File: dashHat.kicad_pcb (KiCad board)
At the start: 4 copper layers, 65 x 56 mm, 114 parts, among them J1 Input, J2 LCD, J3 GPIO, J4 LEDs, J5 SMA, J6 Ride Through, Q1 BSS138, Q2 BSS138, Q3 2N7002, Q4 BSS84, Q5 BSS84, Q6 BSS84, U1 CAT24C256, U2 MAX17614, U3 TVS3300DRV, U4 LM61480, U5 74LVC1G80, U6 ZOE-M8Q, U7 TCAN330, U8 MCP2515-xST, U9 MAX3227, Y1 32.768k, Y2 8MHz

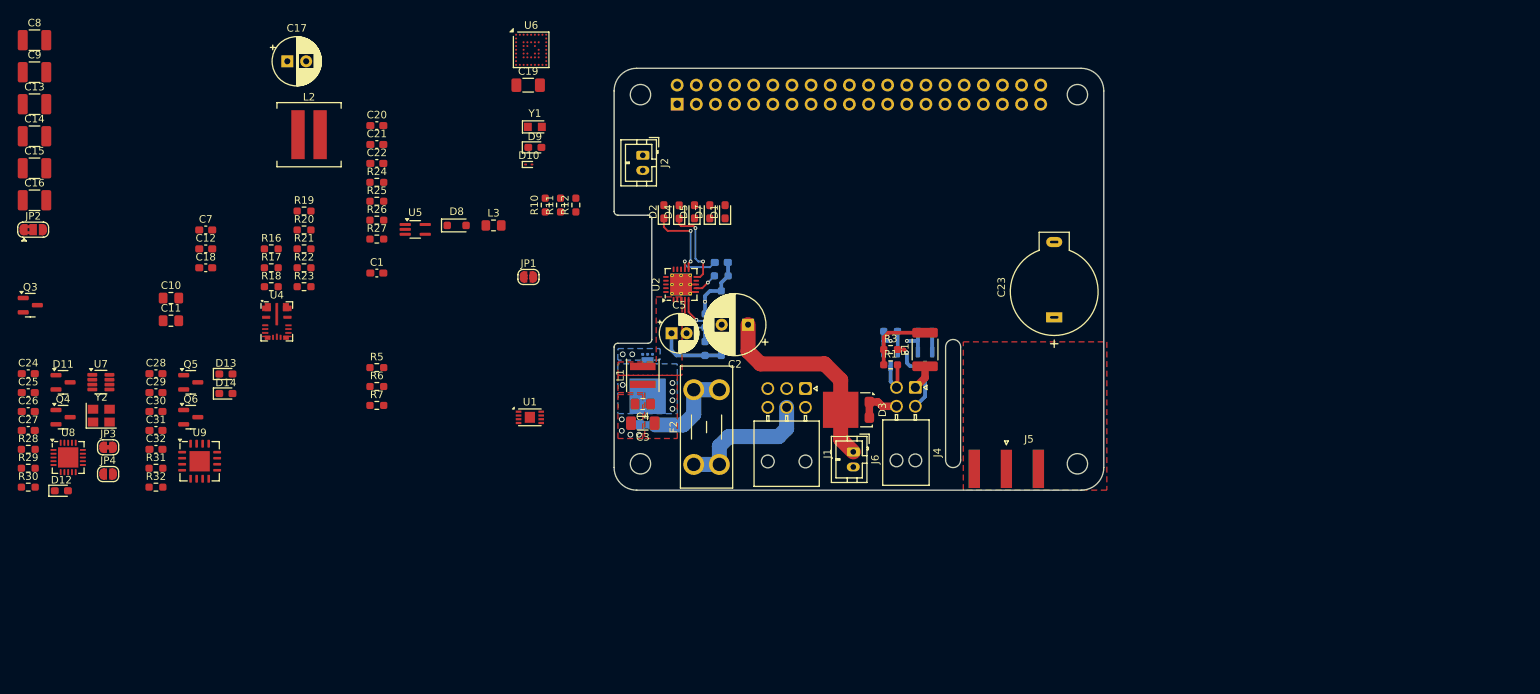
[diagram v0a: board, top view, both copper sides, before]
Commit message: added 4 inputs and 2 pwm outputs, completed routing
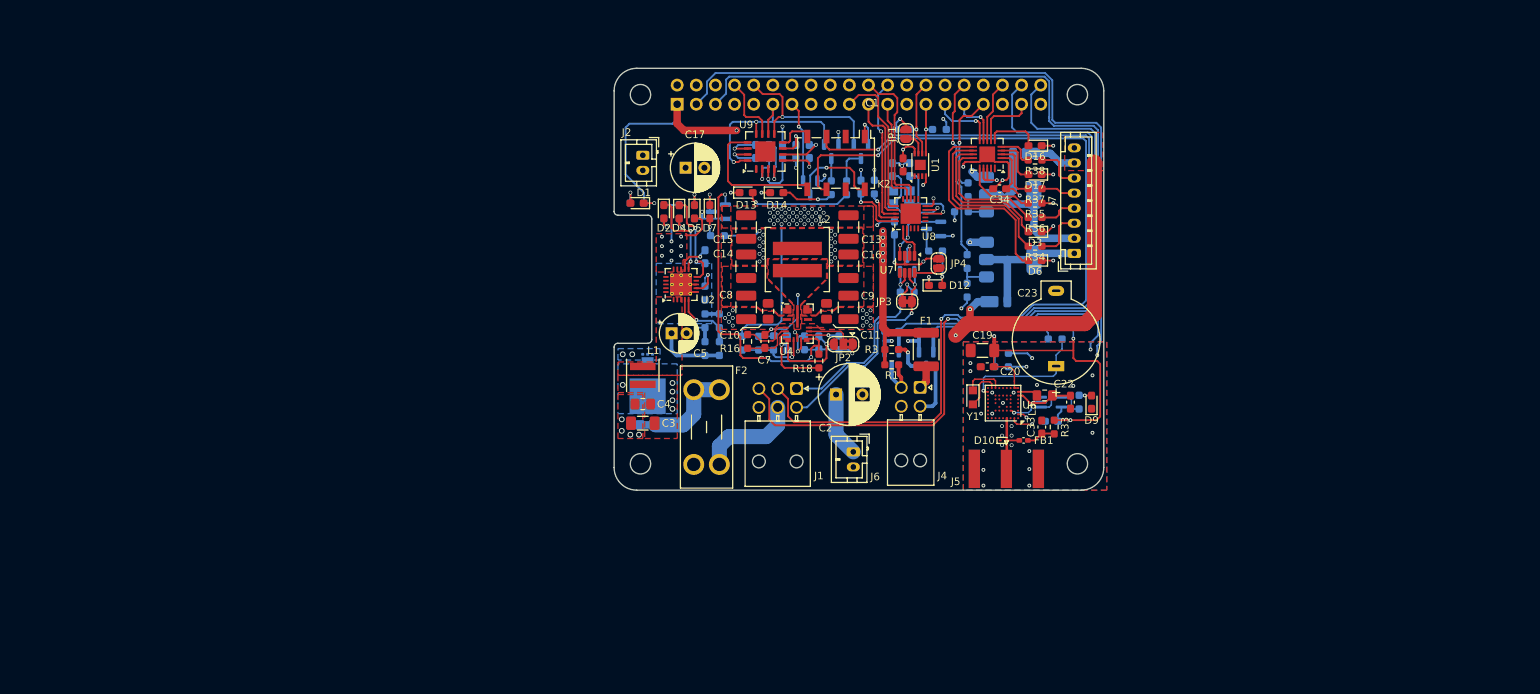
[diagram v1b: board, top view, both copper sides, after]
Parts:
- added C33: 47p, Capacitor_SMD:C_0603_1608Metric_Pad1.08x0.95mm_HandSolder, F.Cu at (156.8, 91.6)
- added C34: 0.1u, Capacitor_SMD:C_0603_1608Metric_Pad1.08x0.95mm_HandSolder, F.Cu at (151.2, 60.0)
- added D16: Green, LED_SMD:LED_0603_1608Metric_Pad1.05x0.95mm_HandSolder, F.Cu at (155.9, 54.3)
- added D17: Green, LED_SMD:LED_0603_1608Metric_Pad1.05x0.95mm_HandSolder, F.Cu at (155.9, 58.1)
- added D18: 60v, 3A, Diode_SMD:D_PowerDI-123, B.Cu at (154.5, 55.3)
- added D19: 60v, 3A, Diode_SMD:D_PowerDI-123, B.Cu at (150.7, 75.0)
- added D6: Green, LED_SMD:LED_0603_1608Metric_Pad1.05x0.95mm_HandSolder, F.Cu at (155.9, 69.5)
- added FB1: 1.8k @ 100MHz, Inductor_SMD:L_0402_1005Metric_Pad0.77x0.64mm_HandSolder, F.Cu at (154.4, 93.4)
- added J7: Conn_01x08, Connector_JST:JST_PH_B8B-PH-K_1x08_P2.00mm_Vertical, F.Cu at (161.1, 68.6)
- added K2: G6K-2, Relay_SMD:Relay_DPDT_Omron_G6K-2F, F.Cu at (129.5, 56.6)
- added Q7: 2N7002, Package_TO_SOT_SMD:SOT-23, B.Cu at (126.0, 59.9)
- added Q8: , Package_TO_SOT_SMD:SOT-223, B.Cu at (152.6, 60.8)
- added Q9: , Package_TO_SOT_SMD:SOT-223, B.Cu at (152.6, 69.4)
- added R33: 10, Resistor_SMD:R_0603_1608Metric_Pad0.98x0.95mm_HandSolder, F.Cu at (158.4, 91.6)
- added R34: 1.5k, Resistor_SMD:R_0603_1608Metric_Pad0.98x0.95mm_HandSolder, F.Cu at (155.9, 67.6)
- added R35: 18k, Resistor_SMD:R_0603_1608Metric_Pad0.98x0.95mm_HandSolder, F.Cu at (155.9, 61.9)
- added R36: 1.5k, Resistor_SMD:R_0603_1608Metric_Pad0.98x0.95mm_HandSolder, F.Cu at (155.9, 63.8)
- added R37: 1.5k, Resistor_SMD:R_0603_1608Metric_Pad0.98x0.95mm_HandSolder, F.Cu at (155.9, 60.0)
- added R38: 1.5k, Resistor_SMD:R_0603_1608Metric_Pad0.98x0.95mm_HandSolder, F.Cu at (155.9, 56.2)
- added R39: 50, Resistor_SMD:R_0603_1608Metric_Pad0.98x0.95mm_HandSolder, B.Cu at (147.0, 60.1)
- added R40: 10k, Resistor_SMD:R_0603_1608Metric_Pad0.98x0.95mm_HandSolder, B.Cu at (146.1, 63.0)
- added R41: 50, Resistor_SMD:R_0603_1608Metric_Pad0.98x0.95mm_HandSolder, B.Cu at (146.9, 69.6)
- added R42: 10k, Resistor_SMD:R_0603_1608Metric_Pad0.98x0.95mm_HandSolder, B.Cu at (146.9, 73.5)
- added U10: MAX22193, Package_DFN_QFN:TQFN-20-1EP_4x4mm_P0.5mm_EP2.1x2.1mm, F.Cu at (149.5, 55.4)
- C12, C18, C21, C24, C25, C26, C27, C28, C29, C30, C31, C32, D11, D8, Q3, Q4, Q5, Q6, R10, R11, R12, R17, R19, R20, R21, R22, R23, R24, R25, R26, R27, R28, R29, R30, R31, R32, R5, R6, R7, U5, Y2: moved to B.Cu
- C6: value 220n -> 1u
- D3: value 100v, 15A -> Green; footprint Package_TO_SOT_SMD:TO-277A -> LED_SMD:LED_0603_1608Metric_Pad1.05x0.95mm_HandSolder
- moved R30 124.5 mm to (142.7, 68.2)
- moved C25 120.7 mm to (139.2, 57.5), turned to 90 degrees
- moved D12 119.2 mm to (142.7, 72.8)
- moved C26 119.1 mm to (137.0, 57.5), turned to 90 degrees
- moved R28 118.5 mm to (138.9, 73.7), turned to 180 degrees
- moved R29 118.4 mm to (134.5, 59.8), turned to 90 degrees
- moved Q4 118.2 mm to (142.4, 65.3), turned to 180 degrees
- moved C24 116.6 mm to (137.2, 65.2), turned to 90 degrees
- moved U8 116.4 mm to (139.4, 63.3), turned to 90 degrees
- moved C27 115.2 mm to (132.8, 59.8), turned to 90 degrees
- moved JP4 113.7 mm to (143.1, 69.9), turned to 90 degrees
- moved D11 113.1 mm to (138.9, 70.0), turned to 90 degrees
- moved C9 112.5 mm to (131.1, 75.7), turned to 90 degrees
- moved Y2 110.1 mm to (138.1, 61.1), turned to 180 degrees
- moved C13 109.3 mm to (131.1, 65.1), turned to 90 degrees
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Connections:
- C10 pad 1: +12V -> VIN
- C11 pad 1: +12V -> VIN
- C2 pad 1: +12V -> VIN
- C8 pad 1: +12V -> VIN
- C9 pad 1: +12V -> VIN
- D3 pad 1: +12V -> GND
- D3 pad 2: GND -> Net-(D3-A)
- D5 pad 1: GND -> Net-(D5-K)
- D5 pad 2: Net-(D5-A) -> VIN
- F2 pad 1: /Power/+12Vraw -> /Power/+12V_{raw}
- J1 pad 1: /RS232/232TX -> /CAN/CANL
- J1 pad 2: /RS232/232RX -> /RS232/232TX
- J1 pad 3: /CAN/CANH -> /RS232/232RX
- J1 pad 4: /CAN/CANL -> /CAN/CANH
- J1 pad 5: /Power/+12Vraw -> /GPIO/+12V_{raw}
- J6 pad 1: +12V -> VIN
- R10 pad 1: +12V -> VIN
- R11 pad 1: +12V -> VIN
- R12 pad 1: +12V -> Net-(D5-K)
- R12 pad 2: Net-(D5-A) -> GND
- U2 pad 13: +12V -> VIN
- U2 pad 14: +12V -> VIN
- U2 pad 15: +12V -> VIN
- U4 pad 13: +12V -> VIN
- U4 pad 14: +12V -> VIN
- U4 pad 2: +12V -> VIN
- U9 pad 13: /RS232/232TX -> Net-(U9-T1OUT)
- U9 pad 8: /RS232/232RX -> Net-(U9-R1IN)
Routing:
- net +3V3: track 7.94 -> 147.6 mm, vias 2 -> 19
- net /RS232/232TX: track 0.00 -> 121.4 mm, vias 0 -> 2
- net /RS232/232RX: track 0.00 -> 120.6 mm, vias 0 -> 2
- net /GPIO2/SDA1: track 0.00 -> 116.8 mm, vias 0 -> 3
- net /GPIO3/SCL1: track 0.00 -> 110.0 mm, vias 0 -> 3
- net /GPIO/+12V_{raw}: track 0.00 -> 102.4 mm, vias 0 -> 2
- net +5V: track 9.39 -> 106.3 mm, vias 0 -> 24
- net GND: track 19.4 -> 95.3 mm, vias 7 -> 94
- net VIN: track 0.00 -> 70.8 mm, vias 0 -> 23
- net /GPIO20/PCM.DIN: track 2.76 -> 69.5 mm
- net /GPIO21/PCM.DOUT: track 2.76 -> 63.3 mm
- net Net-(Q3-G): track 0.00 -> 41.4 mm, vias 0 -> 3
- net /GPIO17: track 0.00 -> 30.7 mm, vias 0 -> 2
- net /CAN/CANH: track 0.00 -> 30.4 mm, vias 0 -> 2
- net +12V: track 27.7 -> 0.00 mm
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- added copper zone on In2.Cu, net +3V3
- added copper zone on F.Cu, net +5V
- added copper zone on In2.Cu, net +5V
- added copper zone on F.Cu, net /GPIO/+12V_{raw}
- added copper zone on F.Cu, net Net-(U4-SW)
- added copper zone on F.Cu, net VIN
- added copper zone on In2.Cu, net VIN
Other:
- outline, holes or cut-outs redrawn
- board text removed: "CAMERA (OPTIONAL)"

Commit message: revised schematic after initial layout  - all connectors are vertical  - increased current handling of outputs  - replaced mechanical relay with ssr  - jumper to disable gps antenna power
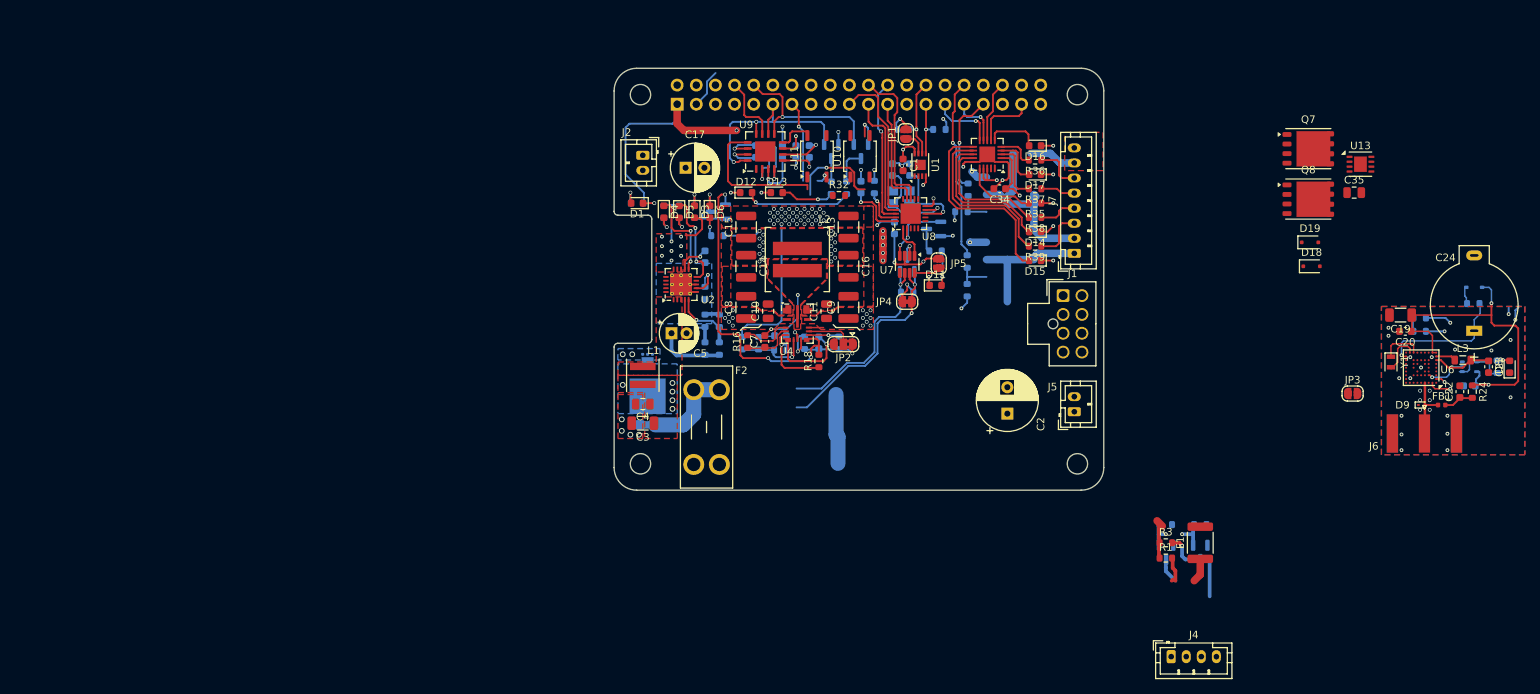
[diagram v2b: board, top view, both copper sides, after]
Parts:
- removed K2: G6K-2, Relay_SMD:Relay_DPDT_Omron_G6K-2F
- removed Q9: , Package_TO_SOT_SMD:SOT-223
- added C35: .47u, Capacitor_SMD:C_0805_2012Metric, F.Cu at (198.2, 60.5)
- added JP3: PA EN, Jumper:SolderJumper-2_P1.3mm_Open_RoundedPad1.0x1.5mm, F.Cu at (198.0, 87.2)
- added R32: 1k, Resistor_SMD:R_0603_1608Metric, F.Cu at (129.8, 60.9)
- added U10: CPC1017N, Package_SO:SOP-4_3.8x4.1mm_P2.54mm, F.Cu at (132.6, 55.7)
- added U11: CPC1017N, Package_SO:SOP-4_3.8x4.1mm_P2.54mm, F.Cu at (126.9, 55.7)
- added U13: IX4427, Package_DFN_QFN:DFN-8-1EP_3x3mm_P0.65mm_EP1.7x2.05mm, F.Cu at (199.1, 56.7)
- C1, C12, C18, C20, C21, C34, C6, C7: footprint Capacitor_SMD:C_0603_1608Metric_Pad1.08x0.95mm_HandSolder -> Capacitor_SMD:C_0603_1608Metric
- C10, C11, C4: footprint Capacitor_SMD:C_0805_2012Metric_Pad1.18x1.45mm_HandSolder -> Capacitor_SMD:C_0805_2012Metric
- C13, C14, C15, C16, C8, C9: footprint Capacitor_SMD:C_1210_3225Metric_Pad1.33x2.70mm_HandSolder -> Capacitor_SMD:C_1210_3225Metric
- C19, C3: footprint Capacitor_SMD:C_1206_3216Metric_Pad1.33x1.80mm_HandSolder -> Capacitor_SMD:C_1206_3216Metric
- C22: renamed from C33; footprint Capacitor_SMD:C_0603_1608Metric_Pad1.08x0.95mm_HandSolder -> Capacitor_SMD:C_0603_1608Metric
- C23: renamed from C22; footprint Capacitor_SMD:C_0603_1608Metric_Pad1.08x0.95mm_HandSolder -> Capacitor_SMD:C_0603_1608Metric
- C25: renamed from C24; footprint Capacitor_SMD:C_0603_1608Metric_Pad1.08x0.95mm_HandSolder -> Capacitor_SMD:C_0603_1608Metric
- C26: renamed from C25; footprint Capacitor_SMD:C_0603_1608Metric_Pad1.08x0.95mm_HandSolder -> Capacitor_SMD:C_0603_1608Metric
- C27: renamed from C26; footprint Capacitor_SMD:C_0603_1608Metric_Pad1.08x0.95mm_HandSolder -> Capacitor_SMD:C_0603_1608Metric
- C28: renamed from C27; footprint Capacitor_SMD:C_0603_1608Metric_Pad1.08x0.95mm_HandSolder -> Capacitor_SMD:C_0603_1608Metric
- C29: renamed from C28; footprint Capacitor_SMD:C_0603_1608Metric_Pad1.08x0.95mm_HandSolder -> Capacitor_SMD:C_0603_1608Metric
- C30: renamed from C29; footprint Capacitor_SMD:C_0603_1608Metric_Pad1.08x0.95mm_HandSolder -> Capacitor_SMD:C_0603_1608Metric
- C31: renamed from C30; footprint Capacitor_SMD:C_0603_1608Metric_Pad1.08x0.95mm_HandSolder -> Capacitor_SMD:C_0603_1608Metric
- C32: renamed from C31; footprint Capacitor_SMD:C_0603_1608Metric_Pad1.08x0.95mm_HandSolder -> Capacitor_SMD:C_0603_1608Metric
- C33: renamed from C32; footprint Capacitor_SMD:C_0603_1608Metric_Pad1.08x0.95mm_HandSolder -> Capacitor_SMD:C_0603_1608Metric
- D1, D16, D17: footprint LED_SMD:LED_0603_1608Metric_Pad1.05x0.95mm_HandSolder -> LED_SMD:LED_0603_1608Metric
- D11: renamed from D12; footprint LED_SMD:LED_0603_1608Metric_Pad1.05x0.95mm_HandSolder -> LED_SMD:LED_0603_1608Metric
- D12: renamed from D13; footprint LED_SMD:LED_0603_1608Metric_Pad1.05x0.95mm_HandSolder -> LED_SMD:LED_0603_1608Metric
- D13: renamed from D14; footprint LED_SMD:LED_0603_1608Metric_Pad1.05x0.95mm_HandSolder -> LED_SMD:LED_0603_1608Metric
- D14: renamed from D3; footprint LED_SMD:LED_0603_1608Metric_Pad1.05x0.95mm_HandSolder -> LED_SMD:LED_0603_1608Metric
- D15: renamed from D6; footprint LED_SMD:LED_0603_1608Metric_Pad1.05x0.95mm_HandSolder -> LED_SMD:LED_0603_1608Metric
- D18, D19: value 60v, 3A -> 40v, 1A; footprint Diode_SMD:D_PowerDI-123 -> Diode_SMD:D_SOD-323F; moved to F.Cu
- D3: renamed from D5; footprint LED_SMD:LED_0603_1608Metric_Pad1.05x0.95mm_HandSolder -> LED_SMD:LED_0603_1608Metric
- D4: renamed from D2; footprint LED_SMD:LED_0603_1608Metric_Pad1.05x0.95mm_HandSolder -> LED_SMD:LED_0603_1608Metric
- D5: renamed from D4; footprint LED_SMD:LED_0603_1608Metric_Pad1.05x0.95mm_HandSolder -> LED_SMD:LED_0603_1608Metric
- D6: renamed from D7; footprint LED_SMD:LED_0603_1608Metric_Pad1.05x0.95mm_HandSolder -> LED_SMD:LED_0603_1608Metric
- D7: renamed from D8; footprint Diode_SMD:D_SOD-323_HandSoldering -> Diode_SMD:D_SOD-323
- D8: renamed from D9; footprint LED_SMD:LED_0603_1608Metric_Pad1.05x0.95mm_HandSolder -> LED_SMD:LED_0603_1608Metric
- F1: footprint Fuse:Fuse_1812_4532Metric_Pad1.30x3.40mm_HandSolder -> Fuse:Fuse_1812_4532Metric
- FB1: footprint Inductor_SMD:L_0402_1005Metric_Pad0.77x0.64mm_HandSolder -> Inductor_SMD:L_0402_1005Metric
- J1: footprint Connector_Molex:Molex_Nano-Fit_105314-xx06_2x03_P2.50mm_Horizontal -> Connector_Molex:Molex_Nano-Fit_105310-xx08_2x04_P2.50mm_Vertical
- J4: footprint Connector_Molex:Molex_Nano-Fit_105314-xx04_2x02_P2.50mm_Horizontal -> Connector_JST:JST_PH_B4B-PH-K_1x04_P2.00mm_Vertical
- L3: footprint Inductor_SMD:L_0805_2012Metric_Pad1.15x1.40mm_HandSolder -> Inductor_SMD:L_0805_2012Metric
- Q7: value 2N7002 -> (none); footprint Package_TO_SOT_SMD:SOT-23 -> Package_SON:Infineon_PG-TDSON-8_6.15x5.15mm; moved to F.Cu
- Q8: footprint Package_TO_SOT_SMD:SOT-223 -> Package_SON:Infineon_PG-TDSON-8_6.15x5.15mm; moved to F.Cu
- R1, R10, R11, R12, R13, R14, R15, R16, R17, R18, R19, R2, R20, R21, R22, R23, R3, R35, R37, R4, R5, R6, R7, R8, R9: footprint Resistor_SMD:R_0603_1608Metric_Pad0.98x0.95mm_HandSolder -> Resistor_SMD:R_0603_1608Metric
- R24: renamed from R33; footprint Resistor_SMD:R_0603_1608Metric_Pad0.98x0.95mm_HandSolder -> Resistor_SMD:R_0603_1608Metric
- R25: renamed from R24; footprint Resistor_SMD:R_0603_1608Metric_Pad0.98x0.95mm_HandSolder -> Resistor_SMD:R_0603_1608Metric
- R26: renamed from R25; footprint Resistor_SMD:R_0603_1608Metric_Pad0.98x0.95mm_HandSolder -> Resistor_SMD:R_0603_1608Metric
- R27: renamed from R26; footprint Resistor_SMD:R_0603_1608Metric_Pad0.98x0.95mm_HandSolder -> Resistor_SMD:R_0603_1608Metric
- R28: renamed from R27; footprint Resistor_SMD:R_0603_1608Metric_Pad0.98x0.95mm_HandSolder -> Resistor_SMD:R_0603_1608Metric
- R29: renamed from R28; footprint Resistor_SMD:R_0603_1608Metric_Pad0.98x0.95mm_HandSolder -> Resistor_SMD:R_0603_1608Metric
- R30: renamed from R29; footprint Resistor_SMD:R_0603_1608Metric_Pad0.98x0.95mm_HandSolder -> Resistor_SMD:R_0603_1608Metric
- R31: renamed from R30; footprint Resistor_SMD:R_0603_1608Metric_Pad0.98x0.95mm_HandSolder -> Resistor_SMD:R_0603_1608Metric
- R33: renamed from R31; footprint Resistor_SMD:R_0603_1608Metric_Pad0.98x0.95mm_HandSolder -> Resistor_SMD:R_0603_1608Metric
- R34: renamed from R32; footprint Resistor_SMD:R_0603_1608Metric_Pad0.98x0.95mm_HandSolder -> Resistor_SMD:R_0603_1608Metric
- R36: renamed from R38; footprint Resistor_SMD:R_0603_1608Metric_Pad0.98x0.95mm_HandSolder -> Resistor_SMD:R_0603_1608Metric
- R38: renamed from R36; footprint Resistor_SMD:R_0603_1608Metric_Pad0.98x0.95mm_HandSolder -> Resistor_SMD:R_0603_1608Metric
- R39: renamed from R34; footprint Resistor_SMD:R_0603_1608Metric_Pad0.98x0.95mm_HandSolder -> Resistor_SMD:R_0603_1608Metric
- R40: renamed from R39; value 50 -> 10; footprint Resistor_SMD:R_0603_1608Metric_Pad0.98x0.95mm_HandSolder -> Resistor_SMD:R_0603_1608Metric
- R41: renamed from R40; footprint Resistor_SMD:R_0603_1608Metric_Pad0.98x0.95mm_HandSolder -> Resistor_SMD:R_0603_1608Metric
- R42: renamed from R41; value 50 -> 10; footprint Resistor_SMD:R_0603_1608Metric_Pad0.98x0.95mm_HandSolder -> Resistor_SMD:R_0603_1608Metric
- R43: renamed from R42; footprint Resistor_SMD:R_0603_1608Metric_Pad0.98x0.95mm_HandSolder -> Resistor_SMD:R_0603_1608Metric
- U5: footprint Package_TO_SOT_SMD:SOT-353_SC-70-5_Handsoldering -> Package_TO_SOT_SMD:SOT-353_SC-70-5
- Y1: footprint Crystal:Crystal_SMD_2012-2Pin_2.0x1.2mm_HandSoldering -> Crystal:Crystal_SMD_2012-2Pin_2.0x1.2mm
- moved Q7 66.3 mm to (192.1, 54.7), turned to 0 degrees
- moved C21 55.7 mm to (213.5, 86.2)
- moved D8 55.7 mm to (218.9, 83.6)
- moved R24 55.7 mm to (213.9, 86.9)
- moved U5 55.7 mm to (213.5, 83.6)
- moved C19 55.7 mm to (204.4, 76.8)
- moved C20 55.7 mm to (205.0, 78.9)
- moved C22 55.7 mm to (212.3, 86.9)
- moved C23 55.7 mm to (216.1, 83.6)
- moved C24 55.7 mm to (214.2, 78.8)
- moved D7 55.7 mm to (214.2, 73.1)
- moved D9 55.7 mm to (207.2, 88.7)
- moved FB1 55.7 mm to (209.9, 88.7)
- moved J6 55.7 mm to (207.6, 92.5)
- moved L3 55.7 mm to (212.6, 82.7)
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- renumbered C23 to C24, D11 to D10, D15 to D2, D10 to D9, J6 to J5, J5 to J6, JP3 to JP4, JP4 to JP5, U10 to U12
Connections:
- C10 pad 1: VIN -> +12V
- C11 pad 1: VIN -> +12V
- C2 pad 1: VIN -> +12V
- C22 pad 1: Net-(C33-Pad1) -> Net-(C22-Pad1)
- C8 pad 1: VIN -> +12V
- C9 pad 1: VIN -> +12V
- D3 pad 2: VIN -> +12V
- D9 pad 2: Net-(D10-A2) -> Net-(D9-A2)
- FB1 pad 1: Net-(D10-A2) -> Net-(JP3-B)
- FB1 pad 2: Net-(C33-Pad1) -> Net-(C22-Pad1)
- J1 pad 1: /CAN/CANL -> /RS232/232TX
- J1 pad 2: /RS232/232TX -> /RS232/232RX
- J1 pad 3: /RS232/232RX -> /CAN/CANH
- J1 pad 4: /CAN/CANH -> /CAN/CANL
- J1 pad 6: GND -> /GPIO/+12V_{raw}
- J5 pad 1: VIN -> +12V
- J6 pad 1: Net-(D10-A2) -> Net-(D9-A2)
- J7 pad 7: /GPIO/+12V_{raw} -> +12V
- J7 pad 8: /GPIO/+12V_{raw} -> +12V
- Q7 pad 1: /GPIO27 -> Net-(Q7-G)
- Q7 pad 2: GND -> Net-(D18-A)
- Q7 pad 3: Net-(Q7-D) -> GND
- Q8 pad 2: Net-(D18-A) -> Net-(D19-A)
- Q8 pad 4: Net-(D18-A) -> Net-(D19-A)
- R10 pad 1: VIN -> +12V
- R11 pad 1: VIN -> +12V
- R24 pad 1: +3V3 -> Net-(C22-Pad1)
- R24 pad 2: Net-(C33-Pad1) -> +3V3
- R40 pad 1: Net-(Q8-G) -> Net-(Q7-G)
- R40 pad 2: /GPIO13/PWM1 -> Net-(U13-~{OUTA})
- R41 pad 1: Net-(Q8-G) -> /GPIO12/PWM0
- R42 pad 1: Net-(Q9-G) -> Net-(Q8-G)
- R42 pad 2: /GPIO12/PWM0 -> Net-(U13-~{OUTB})
- R43 pad 1: Net-(Q9-G) -> /GPIO13/PWM1
- U2 pad 13: VIN -> +12V
- U2 pad 14: VIN -> +12V
- U2 pad 15: VIN -> +12V
- U4 pad 13: VIN -> +12V
- U4 pad 14: VIN -> +12V
- U4 pad 2: VIN -> +12V
- U6 pad A4: Net-(D10-A2) -> Net-(D9-A2)
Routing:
- net /RS232/232TX: track 121.4 -> 0.00 mm, vias 2 -> 0
- net /RS232/232RX: track 120.6 -> 0.00 mm, vias 2 -> 0
- net /GPIO/+12V_{raw}: track 102.4 -> 0.00 mm, vias 2 -> 0
- net /GPIO3/SCL1: track 110.0 -> 21.8 mm
- net /GPIO2/SDA1: track 116.8 -> 31.1 mm
- net VIN: track 70.8 -> 0.00 mm, vias 23 -> 0
- net /GPIO20/PCM.DIN: track 69.5 -> 0.00 mm
- net +12V: track 0.00 -> 68.6 mm, vias 0 -> 23
- net /GPIO21/PCM.DOUT: track 63.3 -> 0.00 mm
- net (no net): track 0.00 -> 30.2 mm, vias 0 -> 1
- net +5V: track 106.3 -> 92.4 mm
- net Net-(Q7-D): track 12.5 -> 0.00 mm, vias 1 -> 0
- net Net-(D10-A2): track 8.43 -> 0.00 mm
- net Net-(Q9-G): track 4.56 -> 0.00 mm
- net Net-(Q7-G): track 0.00 -> 4.44 mm
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- added copper zone on F.Cu, net +12V
- added copper zone on In2.Cu, net +12V
- removed copper zone on F.Cu, net VIN
- removed copper zone on In2.Cu, net VIN
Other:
- board text removed: "PoE"
